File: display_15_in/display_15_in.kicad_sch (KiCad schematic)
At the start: 0 parts

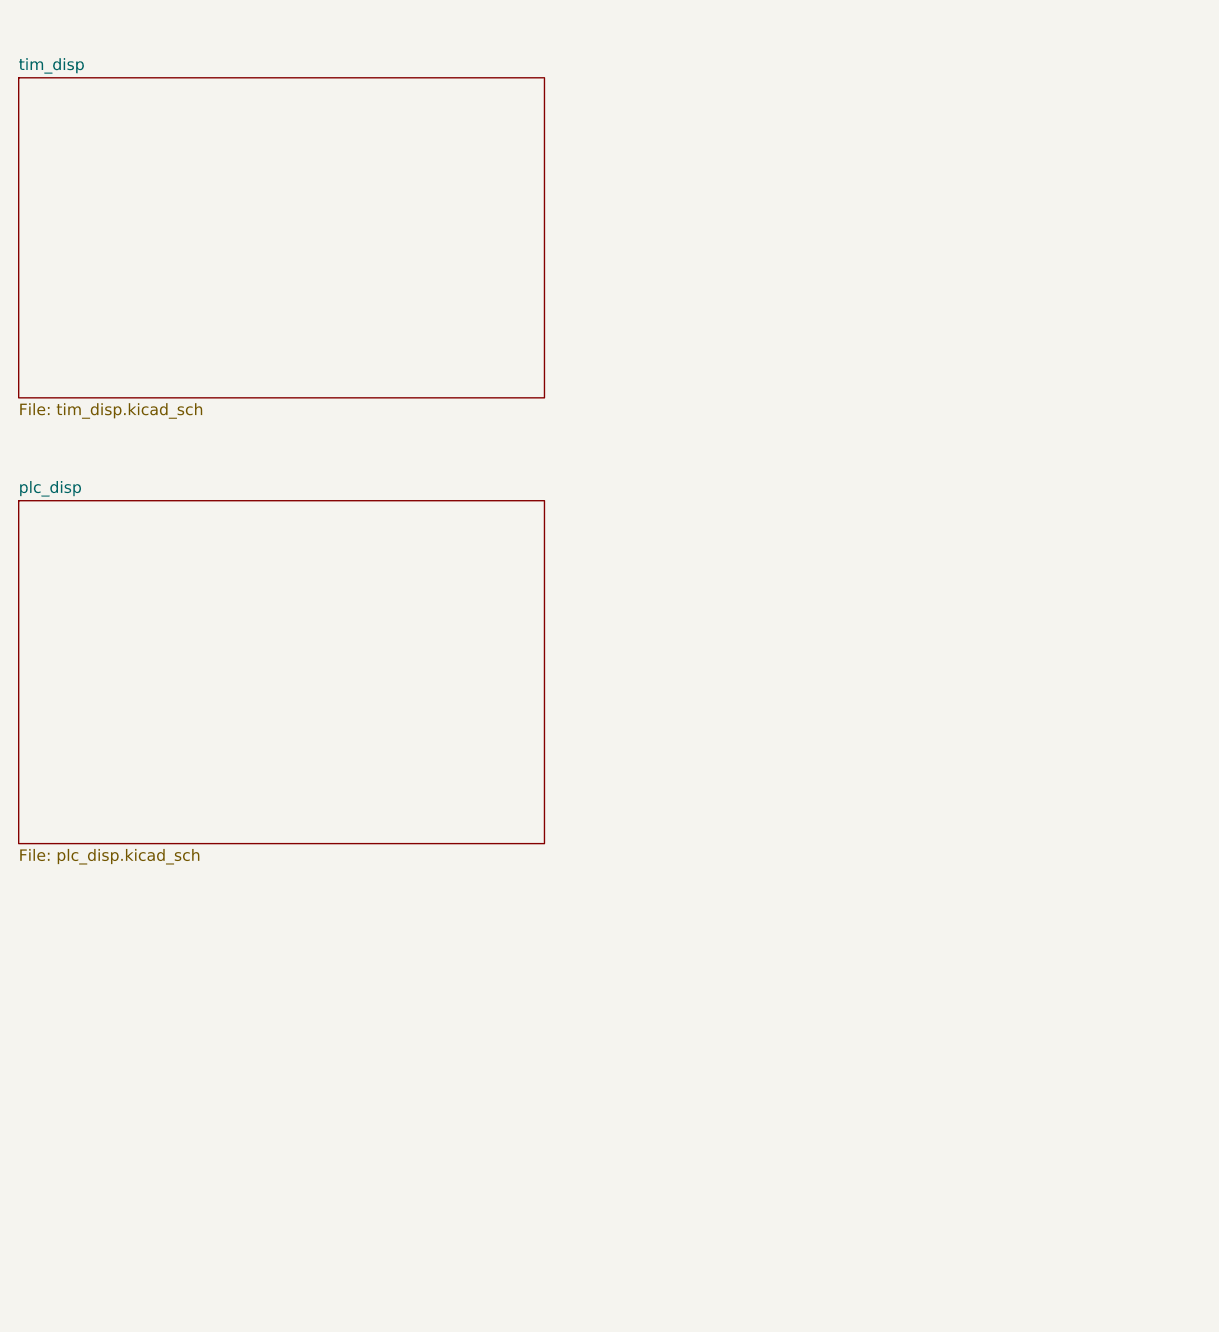
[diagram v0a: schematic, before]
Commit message: added full end of track display board
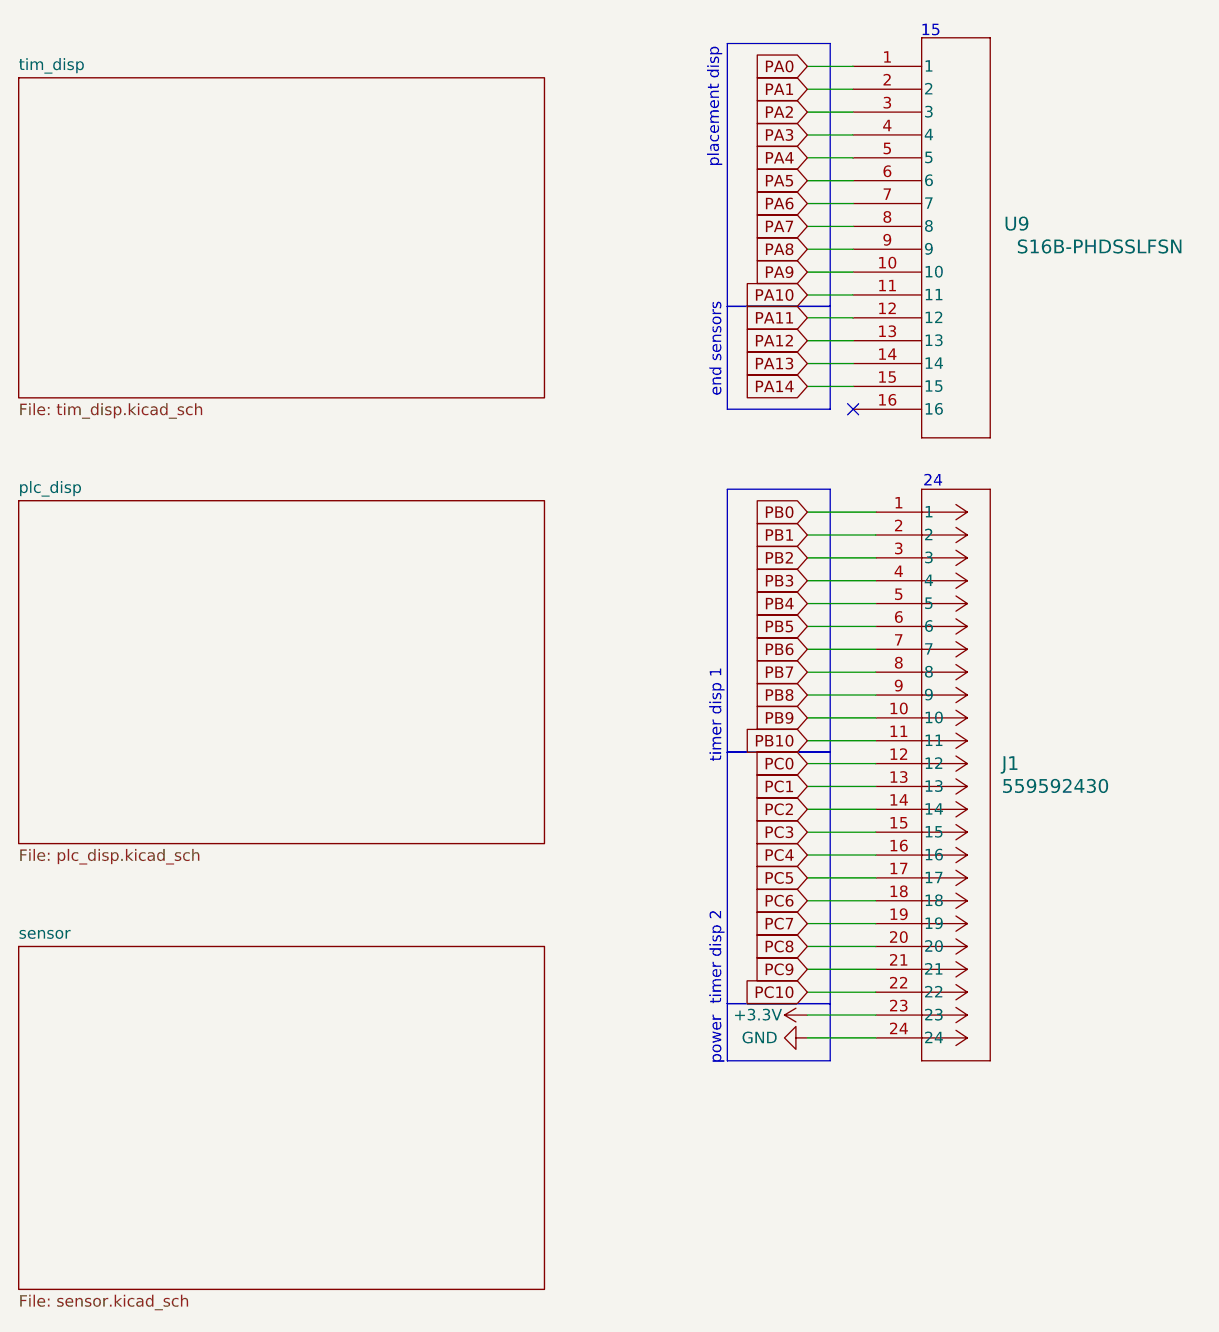
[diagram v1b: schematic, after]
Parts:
- added J1: 559592430, 24pos 2mm:CONN24_559592430_MOL, symbol CONN HEADER 24POS 2MM:559592430
- added U9: S16B-PHDSSLFSN, 16pos 2mm:S16B-PHDSSLFSN_JST, symbol CONN HEADER 16POS 2MM:S16B-PHDSSLFSN
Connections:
- new net +3.3V: J1.23
- new net GND: J1.24
- new net PA0: U9.1
- new net PA1: U9.2
- new net PA10: U9.11
- new net PA11: U9.12
- new net PA12: U9.13
- new net PA13: U9.14
- new net PA14: U9.15
- new net PA2: U9.3
- new net PA3: U9.4
- new net PA4: U9.5
- new net PA5: U9.6
- new net PA6: U9.7
- new net PA7: U9.8
- new net PA8: U9.9
- new net PA9: U9.10
- new net PB0: J1.1
- new net PB1: J1.2
- new net PB10: J1.11
- new net PB2: J1.3
- new net PB3: J1.4
- new net PB4: J1.5
- new net PB5: J1.6
- new net PB6: J1.7
- new net PB7: J1.8
- new net PB8: J1.9
- new net PB9: J1.10
- new net PC0: J1.12
- new net PC1: J1.13
- new net PC10: J1.22
- new net PC2: J1.14
- new net PC3: J1.15
- new net PC4: J1.16
- new net PC5: J1.17
- new net PC6: J1.18
- new net PC7: J1.19
- new net PC8: J1.20
- new net PC9: J1.21
- no-connect marks 0 -> 1
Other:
- added sheet sensor (sensor.kicad_sch)
- note added: "15"
- note added: "24"
- note added: "end sensors"
- note added: "placement disp"
- note added: "power"
- note added: "timer disp 1"
- note added: "timer disp 2"
